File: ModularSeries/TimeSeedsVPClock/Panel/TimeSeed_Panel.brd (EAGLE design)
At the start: 50.5 x 128.5 mm, 14 parts

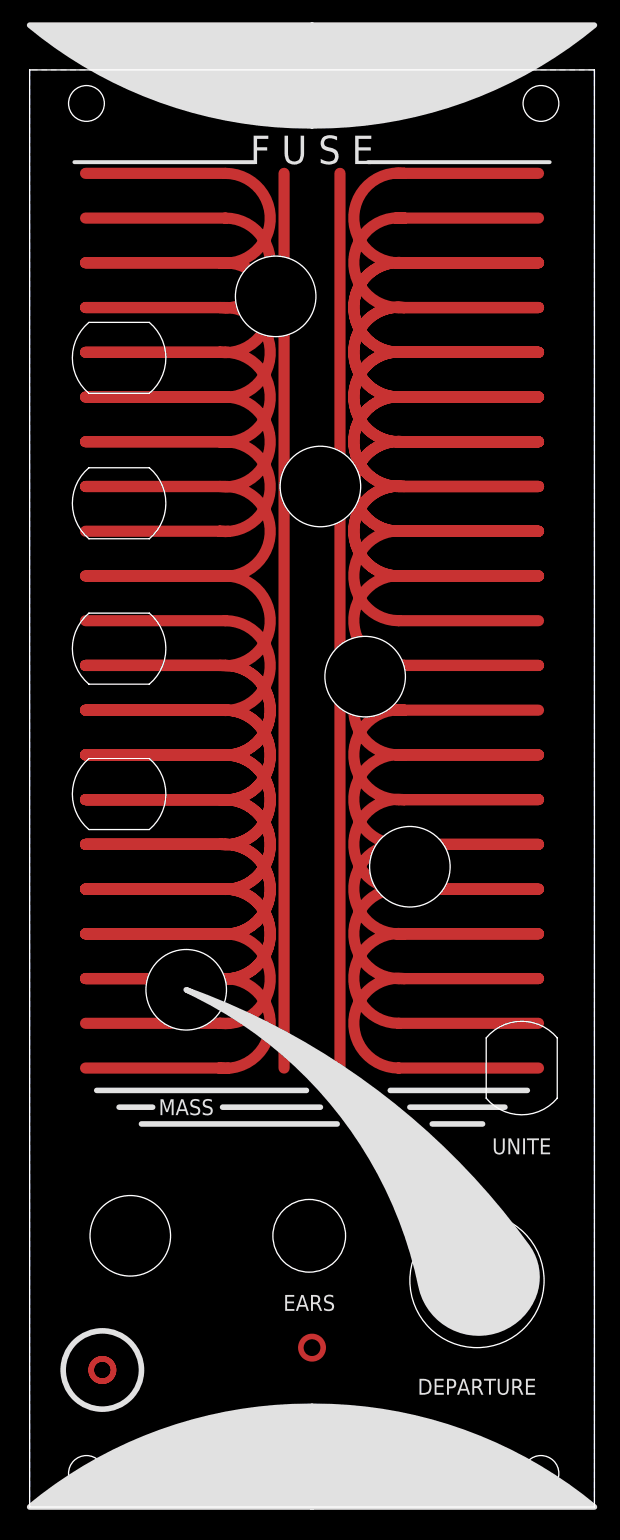
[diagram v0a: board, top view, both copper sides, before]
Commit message: Panel for TimeSeeds added. TLHP core PCB added
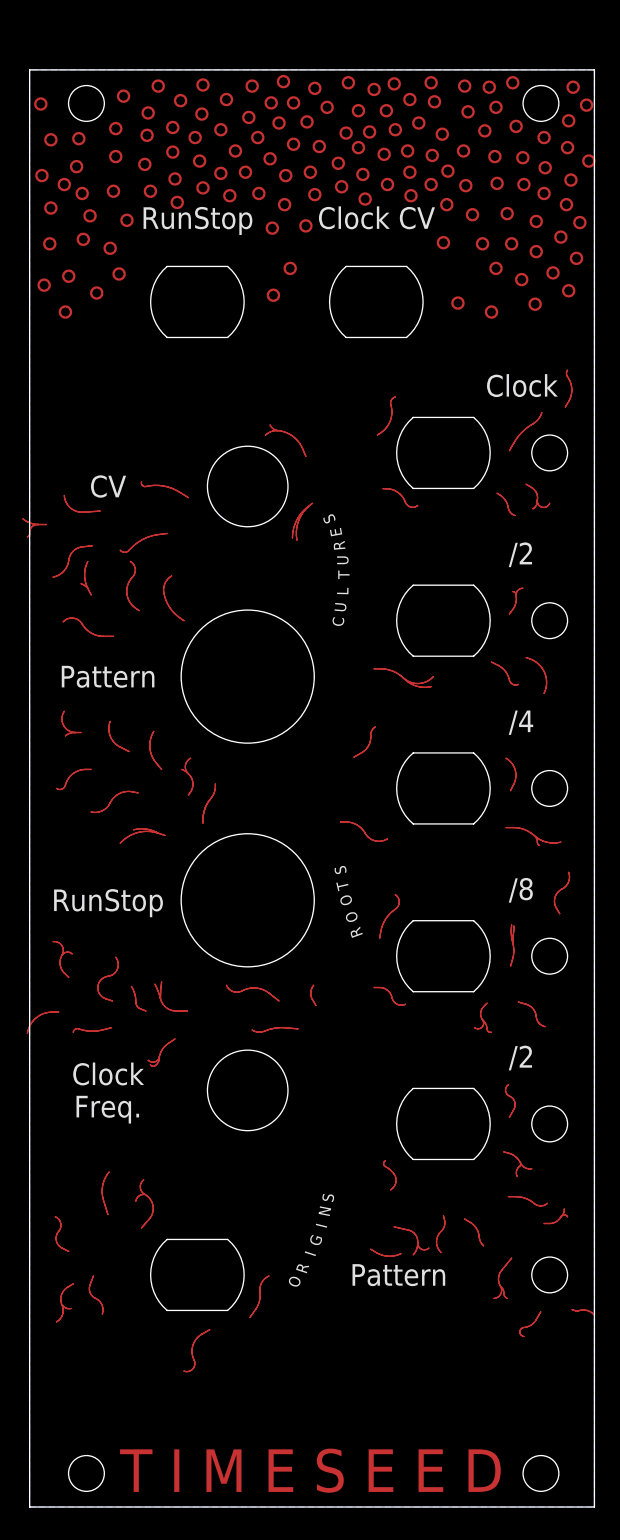
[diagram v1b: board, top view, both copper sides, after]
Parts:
- added E$15, E$16, E$17, E$18: (no value), ElectricNoodleBox:3MMLED_CUTOUT
- added E$19: (no value), ElectricNoodleBox:LOGO20X20
- E$11: device ElectricNoodleBox:ALPHA9MM_POT_CUTOUT -> ElectricNoodleBox:MCDTS_BUTTON_ROUND_CUTOUT
- E$12: device ElectricNoodleBox:MINIJACK_M6_CUTOUT -> ElectricNoodleBox:MCDTS_BUTTON_ROUND_CUTOUT
- E$13: device ElectricNoodleBox:NEUTRIK_6.35_CUTOUT -> ElectricNoodleBox:3MMLED_CUTOUT
- E$14: device ElectricNoodleBox:LOGO20X20 -> ElectricNoodleBox:3MMLED_CUTOUT
- E$2, E$7, E$8: device ElectricNoodleBox:ALPHA9MM_POT_CUTOUT -> ElectricNoodleBox:CINCH_BANANA_CUTOUT
- moved E$13 59.4 mm to (46.5, 65.0)
- moved E$7 58.1 mm to (37.0, 20.0), turned to 90 degrees
- moved E$8 55.6 mm to (15.0, 6.50), turned to 90 degrees
- moved E$11 51.1 mm to (19.5, 60.0)
- moved E$9 37.0 mm to (19.5, 77.0)
- moved E$1 31.8 mm to (15.0, 93.5)
- moved E$4 30.8 mm to (37.0, 65.0)
- moved E$12 30.5 mm to (19.5, 40.0)
- moved E$5 29.0 mm to (37.0, 50.0)
- moved E$3 23.5 mm to (31.0, 93.5)
- moved E$2 20.5 mm to (37.0, 80.0), turned to 90 degrees
- moved E$14 13.5 mm to (46.5, 80.0), flipped to the top
- moved E$6 12.2 mm to (37.0, 35.0), turned to 90 degrees
- moved E$10 10.5 mm to (19.5, 23.0)
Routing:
- net S$2: track 80.0 -> 0.67 mm
- net S$1: track 80.0 -> 2.02 mm
- net S$151: track 12.5 -> 0.36 mm
- net S$107: track 12.5 -> 0.36 mm
- net S$27: track 12.5 -> 0.41 mm
- net S$119: track 12.5 -> 0.50 mm
- net S$99: track 12.5 -> 0.57 mm
- net S$163: track 12.5 -> 0.58 mm
- net S$135: track 12.5 -> 0.60 mm
- net S$171: track 12.5 -> 0.60 mm
- net S$143: track 12.5 -> 0.67 mm
- net S$191: track 12.5 -> 0.70 mm
- net S$87: track 12.5 -> 0.72 mm
- net S$67: track 12.5 -> 0.73 mm
- net S$175: track 12.5 -> 0.76 mm
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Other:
- board text added: "/2"
- board text added: "/4"
- board text added: "/8"
- board text added: "C"
- board text added: "CV"
- board text added: "Clock"
- board text added: "Clock CV"
- board text added: "Clock Freq."
- board text added: "E"
- board text added: "G"
- board text added: "I"
- board text added: "L"
- board text added: "N"
- board text added: "O"
- board text added: "Pattern"
- board text added: "R"
- board text added: "RunStop"
- board text added: "S"
- board text added: "T"
- board text added: "T I M E S E E D"
- board text added: "U"
- board text removed: "DEPARTURE"
- board text removed: "E N D I N G S"
- board text removed: "EARS"
- board text removed: "F U S E"
- board text removed: "MASS"
- board text removed: "UNITE"

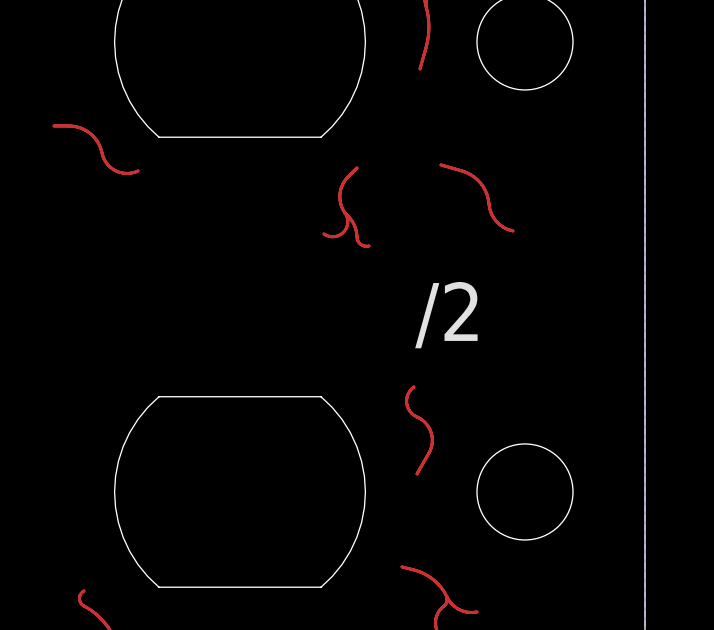
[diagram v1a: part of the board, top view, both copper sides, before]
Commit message: Portals BOM update, Ffrydiau project added
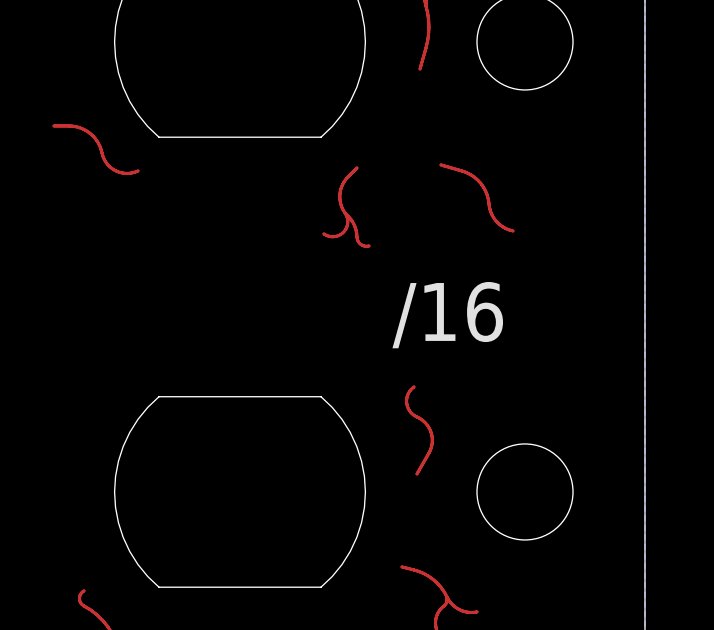
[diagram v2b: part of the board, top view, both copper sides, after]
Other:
- board text added: "/16"
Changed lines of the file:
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@@
 </layers>
 <board>
-<fusionsync huburn="a.cGVyc29uYWw6dWUyYjdlNGE0" projecturn="a.cGVyc29uYWw6dWUyYjdlNGE0IzIwMjAwNDA1MjgzMzA0MTgx" f3durn="urn:adsk.wipprod:dm.lineage:Y39tz4oTQsKUQ-tcbYR8SA" pcbguid="" lastpulledtime="" lastsyncedchangeguid="" latestrevisionid="de486b2f-65fa-41f6-81a7-b63279111559" lastsyncedrevisionid="de486b2f-65fa-41f6-81a7-b63279111559" lastboardhashguid="7055d2db-d7db-5fb8-3466-54cad6186d58" lastpushedtime="2020-06-25T11:17:59Z" linktopcb3d="true"/>
+<fusionsync huburn="a.cGVyc29uYWw6dWUyYjdlNGE0" projecturn="a.cGVyc29uYWw6dWUyYjdlNGE0IzIwMjAwNDA1MjgzMzA0MTgx" f3durn="urn:adsk.wipprod:dm.lineage:Y39tz4oTQsKUQ-tcbYR8SA" pcbguid="" lastpulledtime="" lastsyncedchangeguid="" latestrevisionid="ab122399-fad9-483c-8ff5-5fbf1e069fbb" lastsyncedrevisionid="ab122399-fad9-483c-8ff5-5fbf1e069fbb" lastboardhashguid="5bb234f9-881d-10e4-fa42-a3b30b626d73" lastpushedtime="2020-07-12T20:46:16Z" linktopcb3d="true"/>
 <plain>
 <wire x1="0" y1="-14.25" x2="50.5" y2="-14.25" width="0" layer="20"/>
@@
 <text x="44" y="56" size="1.9304" layer="21" font="vector" ratio="16" align="center">/4</text>
 <text x="44" y="41" size="1.9304" layer="21" font="vector" ratio="16" align="center">/8</text>
-<text x="44" y="26" size="1.9304" layer="21" font="vector" ratio="16" align="center">/2</text>
+<text x="44" y="26" size="1.9304" layer="21" font="vector" ratio="16" align="center">/16</text>
 <text x="33" y="6.5" size="1.9304" layer="21" font="vector" ratio="16" align="center">Pattern</text>
 <text x="7" y="60" size="1.9304" layer="21" font="vector" ratio="16" align="center">Pattern</text>
@@
 <wire x1="16.8" y1="29.5" x2="16.6" y2="29.5" width="1" layer="29"/>
 <wire x1="16.6" y1="29.5" x2="14.4" y2="27.6" width="1" layer="29" curve="81.630164"/>
-<wire x1="8" y1="21.3" x2="6.9" y2="21.6" width="1" layer="29"/>
 <wire x1="8.2" y1="9.2" x2="7.4" y2="9.5" width="1" layer="29"/>
 <wire x1="7.4" y1="9.5" x2="4.7" y2="11.7" width="1" layer="29" curve="-37.235227"/>
